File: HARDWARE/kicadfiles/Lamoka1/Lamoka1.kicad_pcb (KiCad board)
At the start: 2 copper layers, 33 parts

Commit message: Improve on the values for the schematic of boost converter
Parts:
- C1: value C1206C474K5RACTU -> 0.47u
- C2: value CC0603KRX7R9BB223 -> 22n
- C25, C26: value UUX2A470MNL1GS -> 47u
- C27, C32: value UCD2A220MNL1GS -> 22u
- C28: value CL10B104KB8NNNC -> 100n
- C30: value KRM55WR72A226MH01L -> 22u
- C31: value UCD2A101MNJ1MS -> 10u
- Cbst7: value C1206C224M1REC7210 -> 220n
- Cbst8: value C1206C224M1REC7210 -> 0.22u
- Cvcc7: value CNC5L1X7R1H106K160AE -> 100n
- Cvcc8: value CNC5L1X7R1H106K160AE -> 10u
- R1: value RC0603FR-0756K2L -> 56.2k
- R2: value RN73R1JTTD1842F25 -> 18.4k
- R3: value RC0603FR-07392KL -> 392k
- R35, R37, R38: value RC0603FR-0736KL -> 36k
- R39, R40: value TLRP3A30CR005FTE -> 5m
- R4: value RC0603FR-0710KL -> 10k
- R5: value RN73R1JTTD4992F25 -> 49.9k
- moved C25 5.39 mm to (125.7, 106.8)
- moved C26 5.39 mm to (125.7, 118.9)
- moved C27 5.39 mm to (125.7, 131.1)
- moved R40 5.39 mm to (158.4, 127.3)
- moved C1 5.39 mm to (171.1, 128.3)
- moved C2 5.39 mm to (170.3, 131.3)
- moved C28 5.39 mm to (170.2, 133.8)
- moved C30 5.39 mm to (158.2, 133.3)
- moved C31 5.39 mm to (151.9, 110.2)
- moved C32 5.39 mm to (148.1, 124.7)
- moved Cbst7 5.39 mm to (166.3, 121.4)
- moved Cbst8 5.39 mm to (166.3, 124.8)
- moved Cvcc7 5.39 mm to (171.8, 121.3)
- moved Cvcc8 5.39 mm to (171.8, 124.6)
- moved Dbst7 5.39 mm to (165.5, 128.2)
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
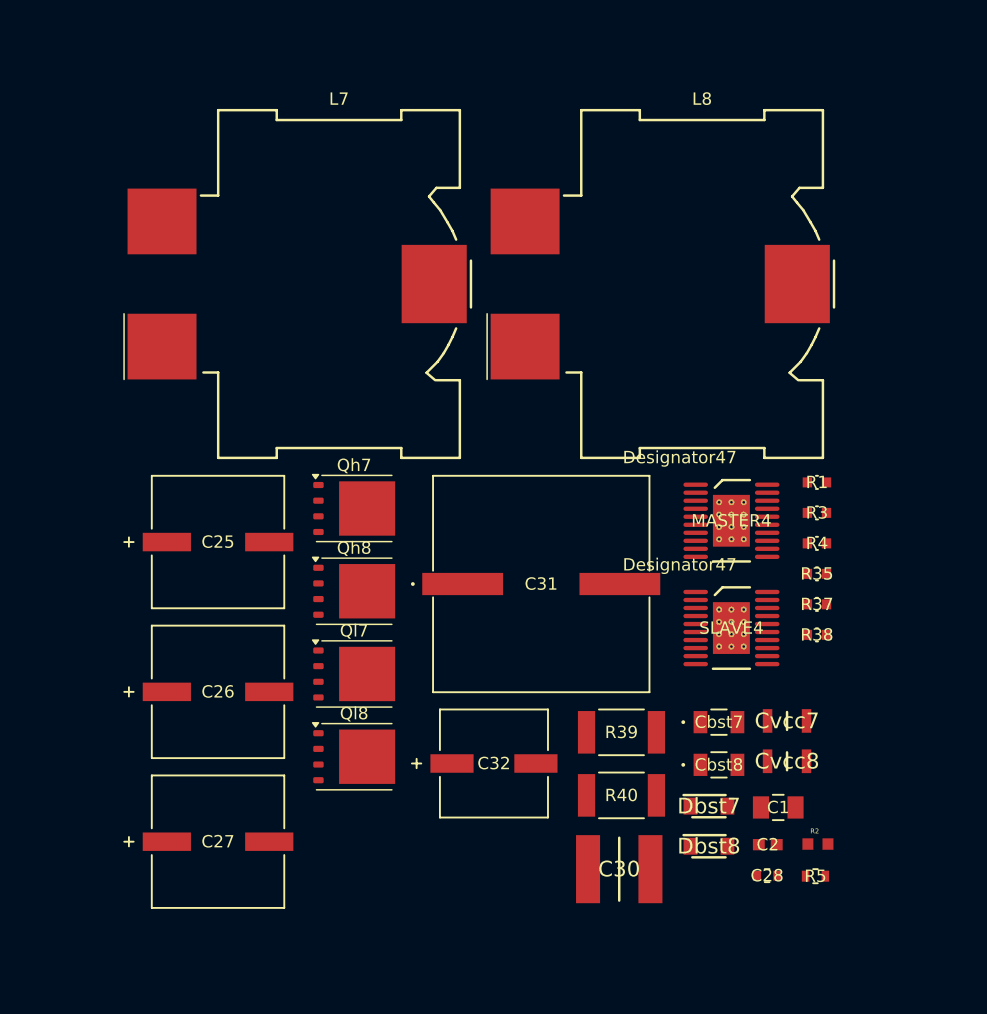
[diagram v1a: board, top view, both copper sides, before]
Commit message: FIX values and add info
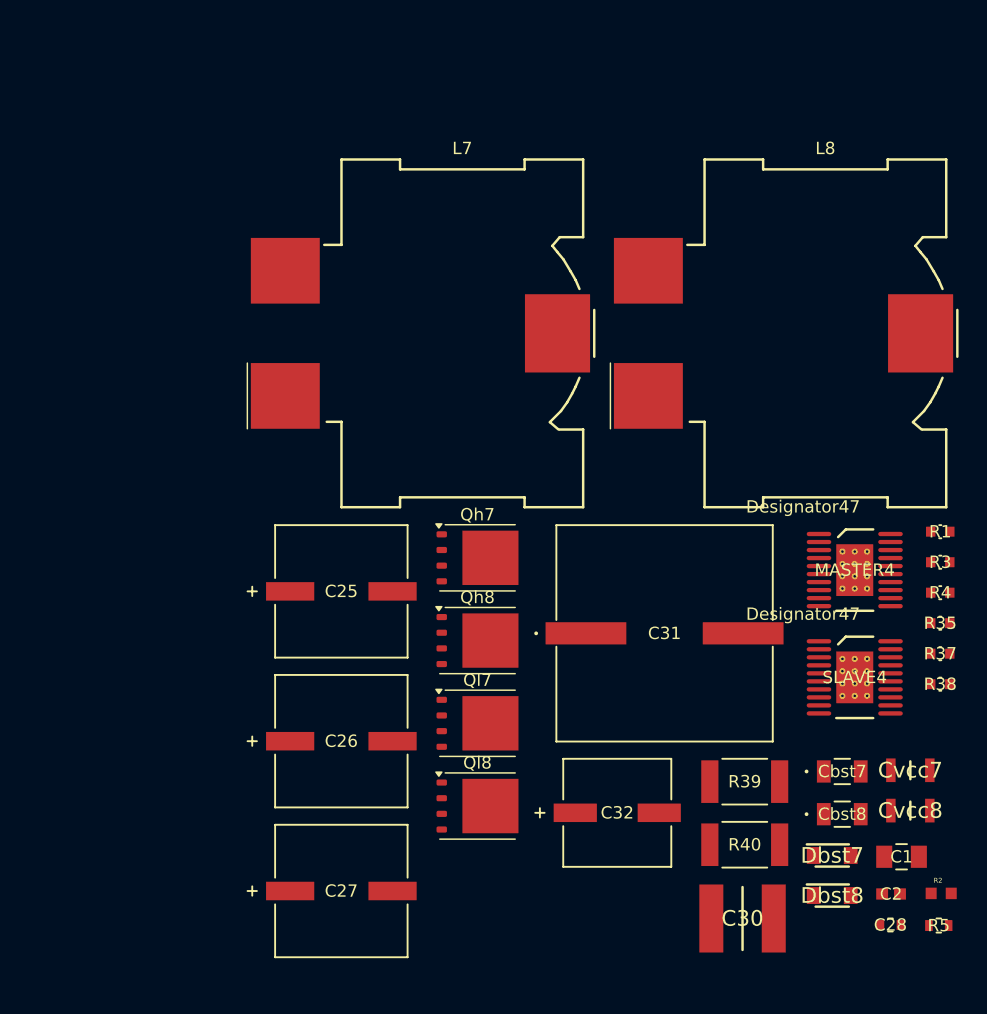
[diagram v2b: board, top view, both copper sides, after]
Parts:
- Cbst7: value 220n -> 0.22u
- Cvcc7: value 100n -> 10u
- moved C25 10.8 mm to (135.7, 110.8)
- moved C26 10.8 mm to (135.7, 122.9)
- moved C27 10.8 mm to (135.7, 135.1)
- moved R40 10.8 mm to (168.4, 131.3)
- moved C1 10.8 mm to (181.1, 132.3)
- moved C2 10.8 mm to (180.3, 135.3)
- moved C28 10.8 mm to (180.2, 137.8)
- moved C30 10.8 mm to (168.2, 137.3)
- moved C31 10.8 mm to (161.9, 114.2)
- moved C32 10.8 mm to (158.1, 128.7)
- moved Cbst7 10.8 mm to (176.3, 125.4)
- moved Cbst8 10.8 mm to (176.3, 128.8)
- moved Cvcc7 10.8 mm to (181.8, 125.3)
- moved Cvcc8 10.8 mm to (181.8, 128.6)
- moved Dbst7 10.8 mm to (175.5, 132.2)
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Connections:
- Qh8 pad 1: Net-(MASTER4-SW) -> Net-(Ql8-D)
- Qh8 pad 2: Net-(MASTER4-SW) -> Net-(Ql8-D)
- Qh8 pad 3: Net-(MASTER4-SW) -> Net-(Ql8-D)
- Ql8 pad 5: Net-(MASTER4-SW) -> Net-(Ql8-D)

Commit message: URGENT had to fix a connection
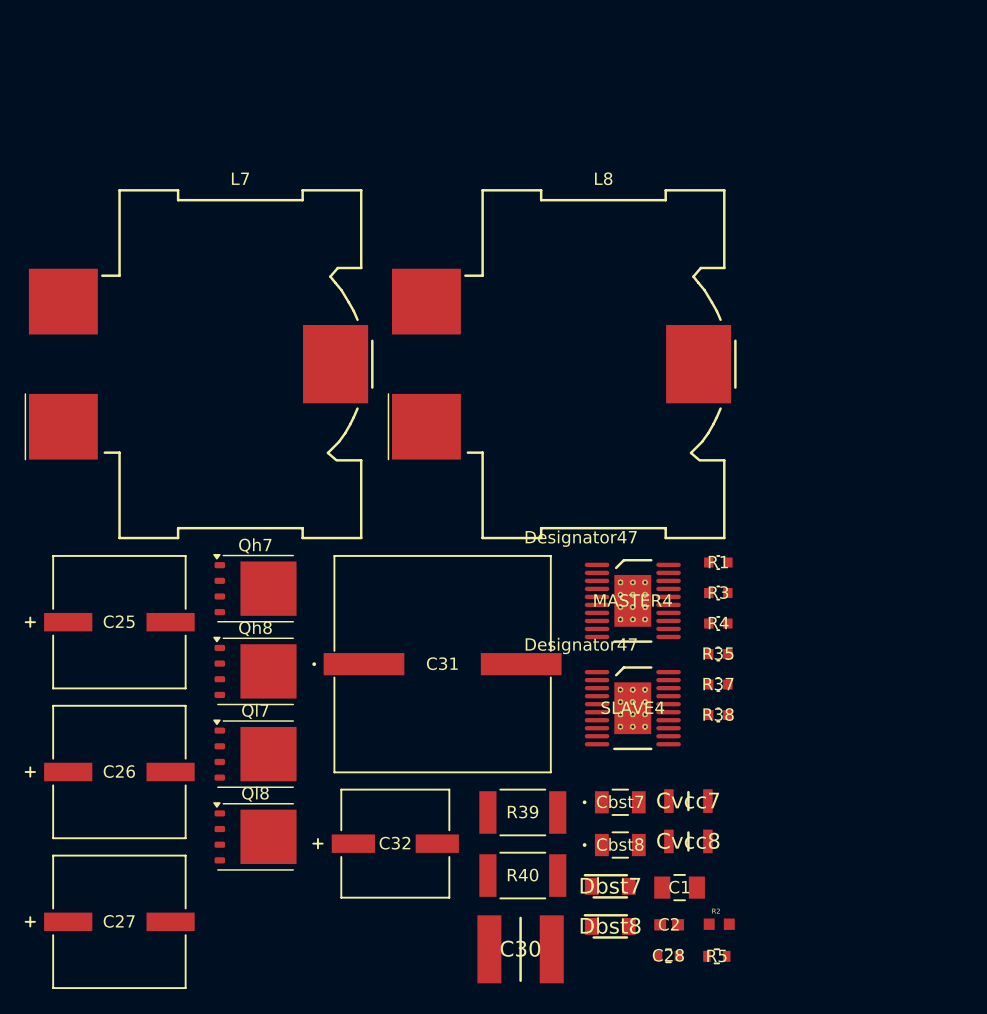
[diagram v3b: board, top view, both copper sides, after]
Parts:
- moved C25 18.2 mm to (117.7, 113.3)
- moved C26 18.2 mm to (117.7, 125.4)
- moved C27 18.2 mm to (117.7, 137.6)
- moved C1 18.2 mm to (163.1, 134.8)
- moved C2 18.2 mm to (162.3, 137.8)
- moved C28 18.2 mm to (162.2, 140.3)
- moved C30 18.2 mm to (150.2, 139.8)
- moved C31 18.2 mm to (143.9, 116.7)
- moved C32 18.2 mm to (140.1, 131.2)
- moved Cbst7 18.2 mm to (158.3, 127.9)
- moved Cbst8 18.2 mm to (158.3, 131.3)
- moved Cvcc7 18.2 mm to (163.8, 127.8)
- moved Cvcc8 18.2 mm to (163.8, 131.1)
- moved Dbst7 18.2 mm to (157.5, 134.7)
- moved Dbst8 18.2 mm to (157.5, 137.9)
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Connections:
- Qh8 pad 1: Net-(Ql8-D) -> Net-(MASTER4-SW)
- Qh8 pad 2: Net-(Ql8-D) -> Net-(MASTER4-SW)
- Qh8 pad 3: Net-(Ql8-D) -> Net-(MASTER4-SW)
- Ql8 pad 5: Net-(Ql8-D) -> Net-(MASTER4-SW)

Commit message: REAL actually fixing it for the net system
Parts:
- removed C28: 100n, Components:CAP_CL10_SAM
- removed C30: 22u, Components:CAPC6153X670N
- removed C31: 10u, Components:CAP_UCD2A_NCH
- removed C32: 22u, Components:PCAP_8x10-ELECT_NCH
- removed R35, R37: 36k, Components:RC0603N_YAG
- added C29: 100n, Components:CAP_CL10_SAM, F.Cu at (144.8, 129.5)
- added C33: 22u, Components:CAPC6153X670N, F.Cu at (160.2, 129.3)
- added C34: 10u, Components:CAP_UCD2A_NCH, F.Cu at (153.9, 106.2)
- added C35: 22u, Components:PCAP_8x10-ELECT_NCH, F.Cu at (150.1, 120.7)
- added R36: 36k, Components:RC0603N_YAG, F.Cu at (176.3, 105.4)
- added R42: 36k, Components:RC0603N_YAG, F.Cu at (176.3, 110.3)
- added U1: AO3400A, Components:SOT-23-3L_AOS, F.Cu at (172.6, 128.7)
- moved R2 24.0 mm to (144.9, 127.0)
- moved R5 21.8 mm to (148.8, 127.1)
- moved R38 16.4 mm to (176.3, 107.8)
- moved C27 14.5 mm to (127.7, 127.1)
- moved R40 14.5 mm to (160.4, 123.3)
- moved C1 14.5 mm to (173.1, 124.3)
- moved C25 14.5 mm to (127.7, 102.8)
- moved C26 14.5 mm to (127.7, 114.9)
- moved Cbst7 14.5 mm to (168.3, 117.4)
- moved Cbst8 14.5 mm to (168.3, 120.8)
- moved Cvcc7 14.5 mm to (173.8, 117.3)
- moved Cvcc8 14.5 mm to (173.8, 120.6)
- moved Dbst7 14.5 mm to (167.5, 124.2)
- moved Dbst8 14.5 mm to (167.5, 127.4)
- moved L7 14.5 mm to (137.5, 81.8)
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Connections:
- net /BOOST-SECTION/VIN-SOURCE renamed /BOOST-SECTION/CSPM
- net Net-(Dbst7-A) renamed /BOOST-SECTION/VCCM
- net Net-(Dbst7-K) renamed /BOOST-SECTION/BSTM
- net Net-(Dbst8-A) renamed /BOOST-SECTION/FBS
- net Net-(Dbst8-K) renamed /BOOST-SECTION/BSTS
- net Net-(MASTER4-COMP) renamed /BOOST-SECTION/COMP
- net Net-(MASTER4-CSN) renamed /BOOST-SECTION/CSNM
- net Net-(MASTER4-FB) renamed /BOOST-SECTION/FBM
- net Net-(MASTER4-HO) renamed /BOOST-SECTION/HOM
- net Net-(MASTER4-LO) renamed /BOOST-SECTION/LOM
- net Net-(MASTER4-MODE) renamed /BOOST-SECTION/MODE
- net Net-(MASTER4-RES) renamed /BOOST-SECTION/RES
- net Net-(MASTER4-SS) renamed /BOOST-SECTION/SS
- net Net-(MASTER4-SW) renamed /BOOST-SECTION/SWM
- net Net-(MASTER4-SYNCOUT) renamed /BOOST-SECTION/SYNCIN/RTS
- net Net-(MASTER4-UVLO) renamed /BOOST-SECTION/UVLO
- net Net-(Qh7-G) renamed /BOOST-SECTION/HOS
- net Net-(Ql7-D) renamed /BOOST-SECTION/SWS
- net Net-(Ql7-G) renamed /BOOST-SECTION/LOS
- net Net-(SLAVE4-CSN) renamed /BOOST-SECTION/CSNS
- net Net-(SLAVE4-SLOPE) renamed /BOOST-SECTION/SLOPES
- MASTER4 pad 12: Net-(MASTER4-SLOPE) -> /BOOST-SECTION/SLOPEM
- MASTER4 pad 8: Net-(MASTER4-SYNCIN/RT) -> /BOOST-SECTION/SYNCIN/RTM

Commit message: ADD more misc "housekeeping" work for boost converter
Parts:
- removed C34: 10u, Components:CAP_UCD2A_NCH
- removed Cbst7, Cbst8: 0.22u, Components:CAP_C1206C-EC_KEM
- removed Cvcc7, Cvcc8: 10u, Components:CAPC3216X190N
- removed Dbst7, Dbst8: SDM1U100S1F-7, Components:SODFL3518X115N
- removed MASTER4, SLAVE4: LM5122QMHE/NOPB, Components:PWP0020A_M
- removed Qh7, Qh8, Ql7, Ql8: CSD19531Q5A, Package_TO_SOT_SMD:TDSON-8-1
- removed U1: AO3400A, Components:SOT-23-3L_AOS
- added C3: 10u, Components:CAPC3216X190N, F.Cu at (180.9, 97.3)
- added C36: 10u, Components:CAP_UCD2A_NCH, F.Cu at (149.7, 105.2)
- added C4: 0.22u, Components:CAP_C1206C-EC_KEM, F.Cu at (154.9, 123.3)
- added C5: 10u, Components:CAPC3216X190N, F.Cu at (180.9, 100.6)
- added C6: 0.22u, Components:CAP_C1206C-EC_KEM, F.Cu at (154.9, 126.7)
- added D7: SDM1U100S1F-7, Components:SODFL3518X115N, F.Cu at (141.4, 126.5)
- added D8: SDM1U100S1F-7, Components:SODFL3518X115N, F.Cu at (141.4, 129.7)
- added Q1: CSD19531Q5A, Package_TO_SOT_SMD:TDSON-8-1, F.Cu at (164.3, 99.1)
- added Q2: CSD19531Q5A, Package_TO_SOT_SMD:TDSON-8-1, F.Cu at (164.3, 105.8)
- added Q3: CSD19531Q5A, Package_TO_SOT_SMD:TDSON-8-1, F.Cu at (164.3, 112.5)
- added Q4: CSD19531Q5A, Package_TO_SOT_SMD:TDSON-8-1, F.Cu at (164.3, 119.2)
- added Q5: AO3400A, Components:SOT-23-3L_AOS, F.Cu at (180.6, 104.9)
- added TP1: Tomachie_TP_N, TestPoint:TestPoint_Pad_D2.0mm, F.Cu at (170.4, 115.1)
- added TP2: Tomachie_TP_S, TestPoint:TestPoint_Pad_D2.0mm, F.Cu at (170.4, 119.2)
- added TP3: Tomachie_TP_N, TestPoint:TestPoint_Pad_D2.0mm, F.Cu at (174.4, 115.1)
- added TP4: Tomachie_TP_N, TestPoint:TestPoint_Pad_D2.0mm, F.Cu at (174.4, 119.2)
- added TP5: Tomachie_TP_N, TestPoint:TestPoint_Pad_D2.0mm, F.Cu at (178.5, 115.1)
- added TP6: Tomachie_TP_W, TestPoint:TestPoint_Pad_D2.0mm, F.Cu at (178.5, 119.2)
- added TP7: Tomachie_TP_W, TestPoint:TestPoint_Pad_D2.0mm, F.Cu at (182.5, 115.1)
- added TP8: Tomachie_TP_W, TestPoint:TestPoint_Pad_D2.0mm, F.Cu at (182.5, 119.2)
- added U2: LM5122QMHE/NOPB, Components:PWP0020A_M, F.Cu at (173.3, 100.0)
- added U3: LM5122QMHE/NOPB, Components:PWP0020A_M, F.Cu at (173.3, 108.8)
- moved R1 32.4 mm to (149.3, 115.9)
- moved R3 32.4 mm to (149.3, 118.4)
- moved R36 32.4 mm to (149.3, 123.3)
- moved R4 32.4 mm to (149.3, 120.8)
- moved R42 32.4 mm to (149.3, 128.3)
- moved R38 32.4 mm to (149.3, 125.8)
- moved C35 26.1 mm to (175.6, 126.3)
- moved R39 17.4 mm to (143.0, 117.2)
- moved R40 17.4 mm to (143.0, 122.3)
- moved C1 17.0 mm to (181.2, 109.3)
- moved R5 13.7 mm to (162.1, 123.8)
- moved C2 13.5 mm to (153.3, 129.7)
- moved R2 12.8 mm to (157.4, 129.7)
- moved C33 12.2 mm to (155.5, 118.1)
- moved C29 4.66 mm to (149.3, 130.7)
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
